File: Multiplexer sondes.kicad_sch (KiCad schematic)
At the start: 4 parts

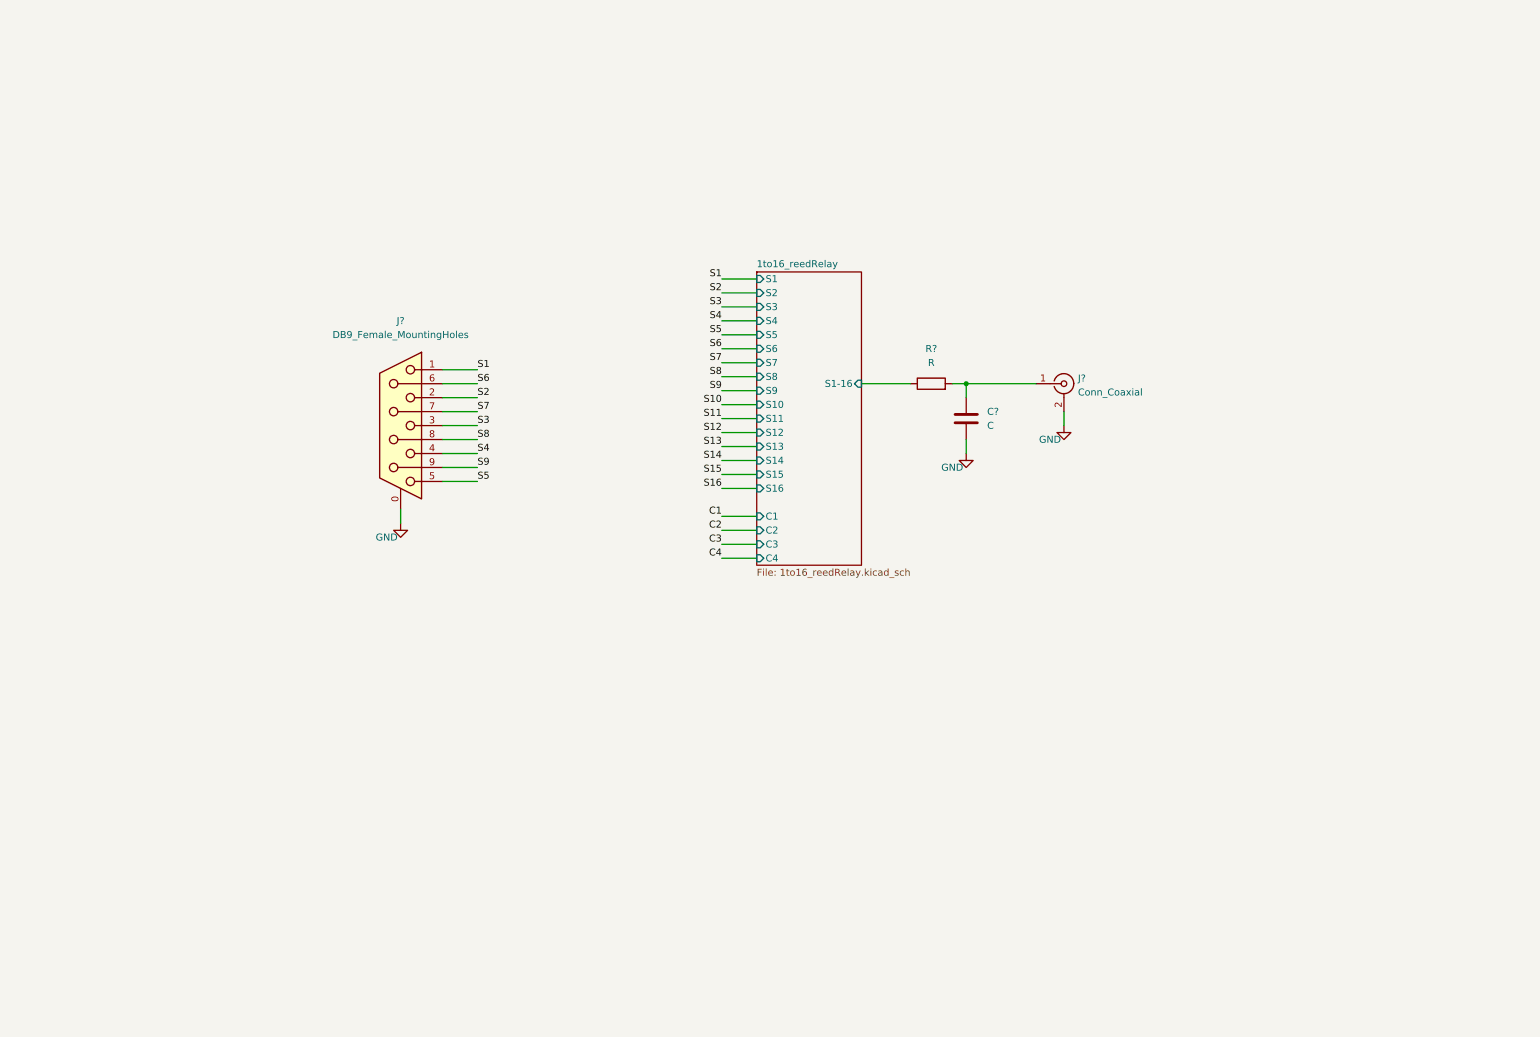
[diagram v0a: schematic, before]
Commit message: Changed to COMUS relay (sch & pcb) 1st placement
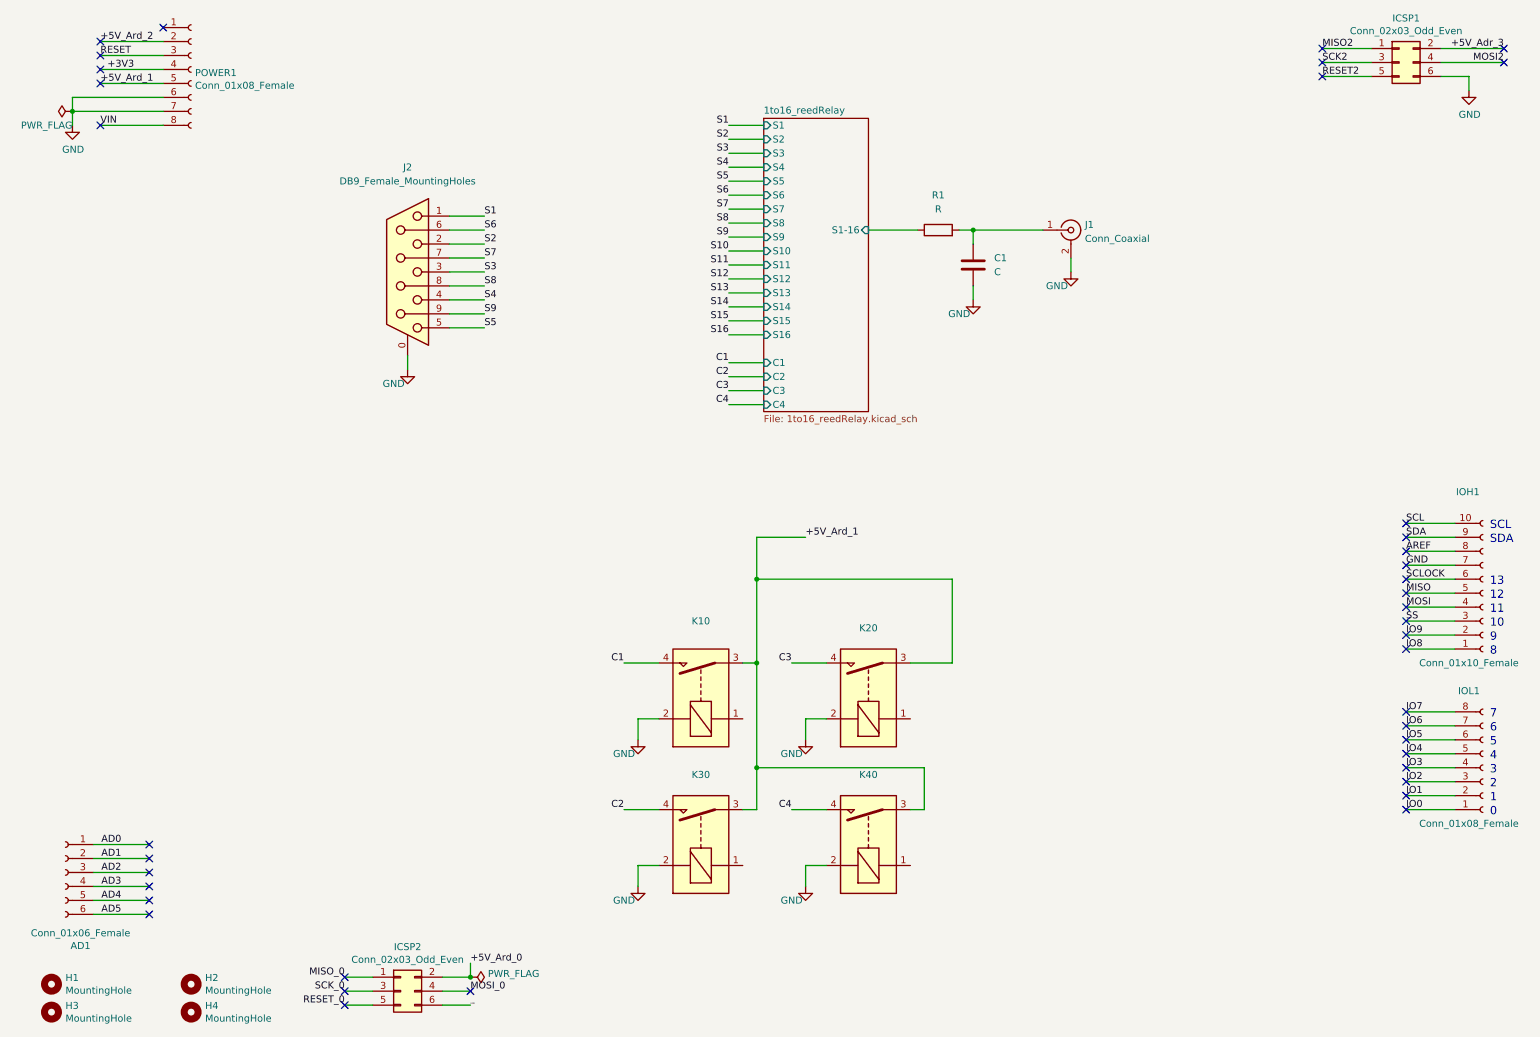
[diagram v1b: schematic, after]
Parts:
- added AD1: Conn_01x06_Female, Connector_PinHeader_2.54mm:PinHeader_1x06_P2.54mm_Vertical, symbol Connector:Conn_01x06_Female
- added H1, H2, H3, H4: MountingHole, MountingHole:MountingHole_3mm, symbol Mechanical:MountingHole
- added ICSP1, ICSP2: Conn_02x03_Odd_Even, Connector_PinSocket_2.54mm:PinSocket_2x03_P2.54mm_Vertical, symbol Connector_Generic:Conn_02x03_Odd_Even
- added IOH1: Conn_01x10_Female, Connector_PinHeader_2.54mm:PinHeader_1x10_P2.54mm_Vertical, symbol Connector:Conn_01x10_Female
- added IOL1, POWER1: Conn_01x08_Female, Connector_PinHeader_2.54mm:PinHeader_1x08_P2.54mm_Vertical, symbol Connector:Conn_01x08_Female
- added K10, K20, K30, K40: (no value), symbol LibPersoNadj:Relay_reed_SPST_1A_small
- C1: renamed from C?; footprint (none) -> Capacitor_SMD:C_0603_1608Metric_Pad1.08x0.95mm_HandSolder
- J1: renamed from J?; footprint (none) -> Connector_Coaxial:SMA_Molex_73251-2120_EdgeMount_Horizontal
- J2: renamed from J?; footprint (none) -> Connector_Dsub:DSUB-9_Female_Horizontal_P2.77x2.84mm_EdgePinOffset4.94mm_Housed_MountingHolesOffset7.48mm
- R1: renamed from R?; footprint (none) -> Resistor_SMD:R_0603_1608Metric_Pad0.98x0.95mm_HandSolder
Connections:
- net C1: now also K10.4
- net C2: now also K30.4
- net C3: now also K20.4
- net C4: now also K40.4
- net GND: now also ICSP1.6 (Pin_6), ICSP2.6 (Pin_6), IOH1.7 (Pin_7), K10.2, K20.2, K30.2, K40.2, POWER1.6 (Pin_6), POWER1.7 (Pin_7)
- new net +3V3: POWER1.4 (Pin_4)
- new net +5V_Adr_3: ICSP1.2 (Pin_2)
- new net +5V_Ard_0: ICSP2.2 (Pin_2)
- new net +5V_Ard_1: K10.3, K20.3, K30.3, K40.3, POWER1.5 (Pin_5)
- new net +5V_Ard_2: POWER1.2 (Pin_2)
- new net AD0: AD1.1 (Pin_1)
- new net AD1: AD1.2 (Pin_2)
- new net AD2: AD1.3 (Pin_3)
- new net AD3: AD1.4 (Pin_4)
- new net AD4: AD1.5 (Pin_5)
- new net AD5: AD1.6 (Pin_6)
- new net AREF: IOH1.8 (Pin_8)
- new net IO0: IOL1.1 (Pin_1)
- new net IO1: IOL1.2 (Pin_2)
- new net IO2: IOL1.3 (Pin_3)
- new net IO3: IOL1.4 (Pin_4)
- new net IO4: IOL1.5 (Pin_5)
- new net IO5: IOL1.6 (Pin_6)
- new net IO6: IOL1.7 (Pin_7)
- new net IO7: IOL1.8 (Pin_8)
- new net IO8: IOH1.1 (Pin_1)
- new net IO9: IOH1.2 (Pin_2)
- new net MISO: IOH1.5 (Pin_5)
- new net MISO2: ICSP1.1 (Pin_1)
- new net MISO_0: ICSP2.1 (Pin_1)
- new net MOSI: IOH1.4 (Pin_4)
- new net MOSI2: ICSP1.4 (Pin_4)
- new net MOSI_0: ICSP2.4 (Pin_4)
- new net RESET: POWER1.3 (Pin_3)
- new net RESET2: ICSP1.5 (Pin_5)
- new net RESET_0: ICSP2.5 (Pin_5)
- new net SCK2: ICSP1.3 (Pin_3)
- new net SCK_0: ICSP2.3 (Pin_3)
- new net SCL: IOH1.10 (Pin_10)
- new net SCLOCK: IOH1.6 (Pin_6)
- new net SDA: IOH1.9 (Pin_9)
- new net SS: IOH1.3 (Pin_3)
- new net VIN: POWER1.8 (Pin_8)
- no-connect marks 0 -> 39
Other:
- note added: "0"
- note added: "1"
- note added: "10"
- note added: "11"
- note added: "12"
- note added: "13"
- note added: "2"
- note added: "3"
- note added: "4"
- note added: "5"
- note added: "6"
- note added: "7"
- note added: "8"
- note added: "9"
- note added: "SCL"
- note added: "SDA"
- moved on the sheet: C1, J1, J2, R1

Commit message: deleted part of the arduino's pins began routing
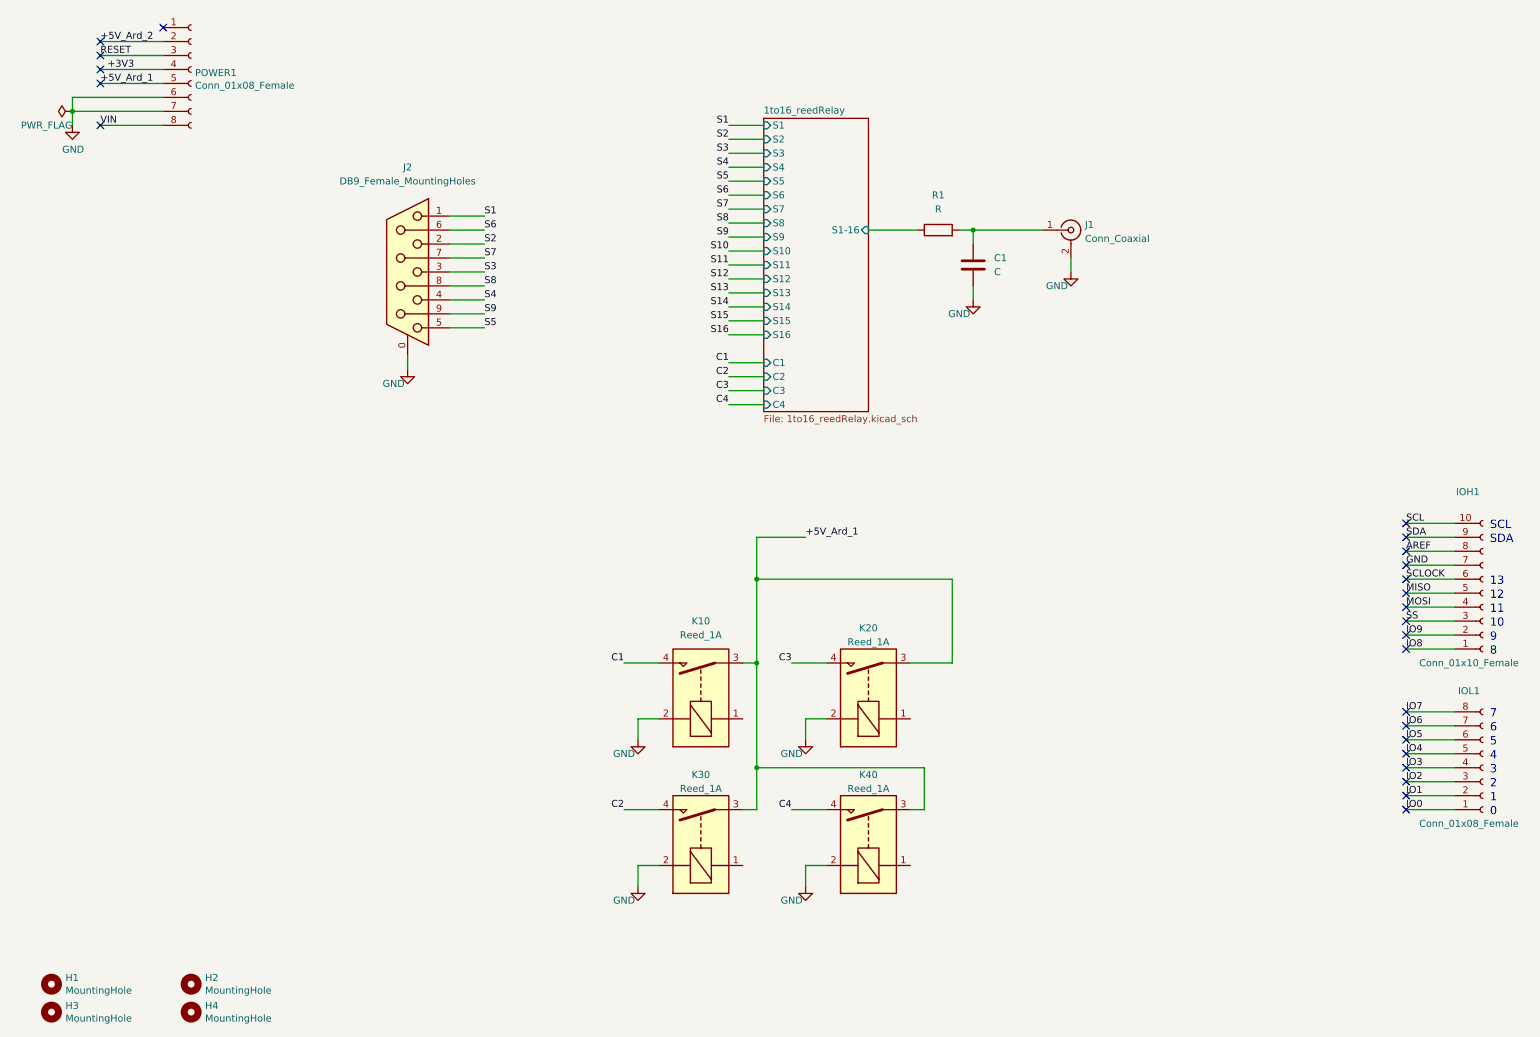
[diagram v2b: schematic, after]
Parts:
- removed AD1: Conn_01x06_Female, Connector_PinHeader_2.54mm:PinHeader_1x06_P2.54mm_Vertical, symbol Connector:Conn_01x06_Female
- removed ICSP1, ICSP2: Conn_02x03_Odd_Even, Connector_PinSocket_2.54mm:PinSocket_2x03_P2.54mm_Vertical, symbol Connector_Generic:Conn_02x03_Odd_Even
- K10, K20, K30, K40: value (none) -> Reed_1A; footprint (none) -> LibPersoNadj:Relay_reed_comus_3570-1517
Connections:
- no-connect marks 39 -> 24

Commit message: Passed to 1 relay per signal with Arduino Mega
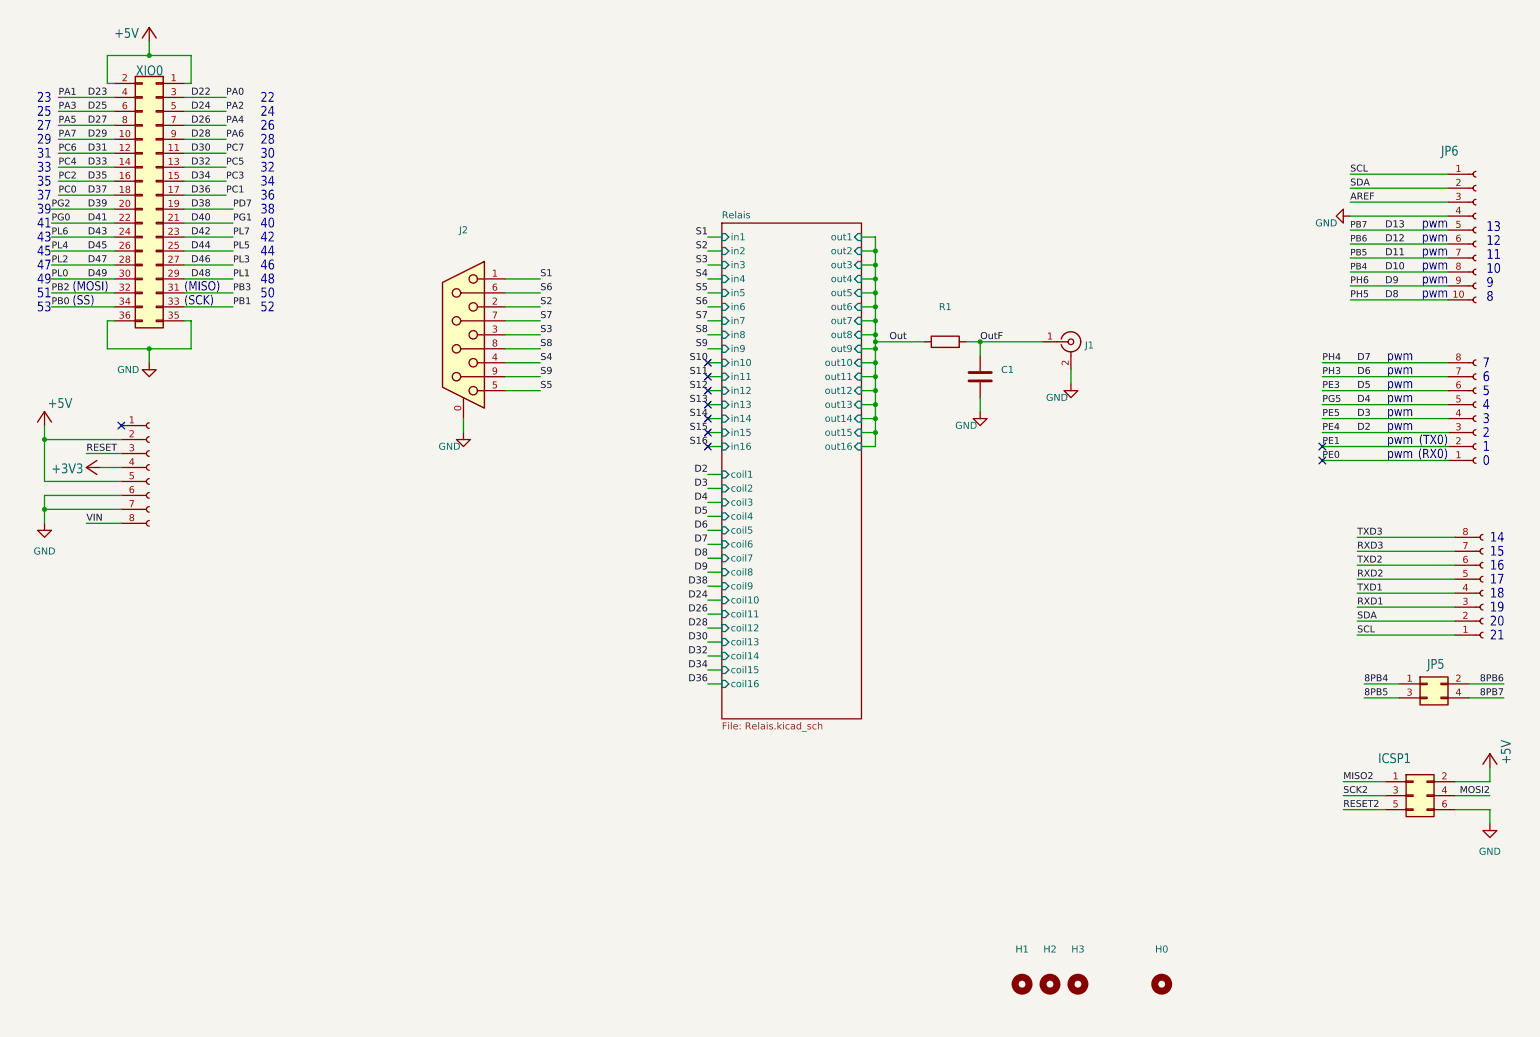
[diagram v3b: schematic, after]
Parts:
- removed H4: MountingHole, MountingHole:MountingHole_3mm, symbol Mechanical:MountingHole
- removed IOH1: Conn_01x10_Female, Connector_PinHeader_2.54mm:PinHeader_1x10_P2.54mm_Vertical, symbol Connector:Conn_01x10_Female
- removed IOL1, POWER1: Conn_01x08_Female, Connector_PinHeader_2.54mm:PinHeader_1x08_P2.54mm_Vertical, symbol Connector:Conn_01x08_Female
- removed K10, K20, K30, K40: Reed_1A, LibPersoNadj:Relay_reed_comus_3570-1517, symbol LibPersoNadj:Relay_reed_SPST_1A_small
- added COMMUNICATION0, POWER0, PWML0: (no value), symbol Connector:Conn_01x08_Female
- added H0: (no value), symbol Mechanical:MountingHole
- added ICSP1: (no value), symbol Connector_Generic:Conn_02x03_Odd_Even
- added JP5: (no value), symbol Connector_Generic:Conn_02x02_Odd_Even
- added JP6: (no value), symbol Connector:Conn_01x10_Female
- added XIO0: (no value), symbol Connector_Generic:Conn_02x18_Odd_Even
- C1: value C -> (none); footprint Capacitor_SMD:C_0603_1608Metric_Pad1.08x0.95mm_HandSolder -> (none)
- H1, H2, H3: value MountingHole -> (none); footprint MountingHole:MountingHole_3mm -> (none)
- J1: value Conn_Coaxial -> (none); footprint Connector_Coaxial:SMA_Molex_73251-2120_EdgeMount_Horizontal -> (none)
- J2: value DB9_Female_MountingHoles -> (none); footprint Connector_Dsub:DSUB-9_Female_Horizontal_P2.77x2.84mm_EdgePinOffset4.94mm_Housed_MountingHolesOffset7.48mm -> (none)
- R1: value R -> (none); footprint Resistor_SMD:R_0603_1608Metric_Pad0.98x0.95mm_HandSolder -> (none)
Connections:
- net +3V3: now also POWER0.4 (Pin_4)
- net AREF: now also JP6.3 (Pin_3)
- net GND: now also ICSP1.6 (Pin_6), JP6.4 (Pin_4), POWER0.6 (Pin_6), POWER0.7 (Pin_7), XIO0.35 (Pin_35), XIO0.36 (Pin_36)
- net RESET: now also POWER0.3 (Pin_3)
- net SCL: now also COMMUNICATION0.1 (Pin_1), JP6.1 (Pin_1)
- net SDA: now also COMMUNICATION0.2 (Pin_2), JP6.2 (Pin_2)
- net VIN: now also POWER0.8 (Pin_8)
- net OutF: now reaches C1.1, J1.1 (In), R1.2
- net 1to16_reedRelay/S1-16 renamed Out
- new net +5V: ICSP1.2 (Pin_2), POWER0.2 (Pin_2), POWER0.5 (Pin_5), XIO0.1 (Pin_1), XIO0.2 (Pin_2)
- new net 8PB4: JP5.1 (Pin_1)
- new net 8PB5: JP5.3 (Pin_3)
- new net 8PB6: JP5.2 (Pin_2)
- new net 8PB7: JP5.4 (Pin_4)
- new net D10: JP6.8 (Pin_8)
- new net D11: JP6.7 (Pin_7)
- new net D12: JP6.6 (Pin_6)
- new net D13: JP6.5 (Pin_5)
- new net D2: PWML0.3 (Pin_3)
- new net D22: XIO0.3 (Pin_3)
- new net D23: XIO0.4 (Pin_4)
- new net D24: XIO0.5 (Pin_5)
- new net D25: XIO0.6 (Pin_6)
- new net D26: XIO0.7 (Pin_7)
- new net D27: XIO0.8 (Pin_8)
- new net D28: XIO0.9 (Pin_9)
- new net D29: XIO0.10 (Pin_10)
- new net D3: PWML0.4 (Pin_4)
- new net D30: XIO0.11 (Pin_11)
- new net D31: XIO0.12 (Pin_12)
- new net D32: XIO0.13 (Pin_13)
- new net D33: XIO0.14 (Pin_14)
- new net D34: XIO0.15 (Pin_15)
- new net D35: XIO0.16 (Pin_16)
- new net D36: XIO0.17 (Pin_17)
- new net D37: XIO0.18 (Pin_18)
- new net D38: XIO0.19 (Pin_19)
- new net D39: XIO0.20 (Pin_20)
- new net D4: PWML0.5 (Pin_5)
- new net D40: XIO0.21 (Pin_21)
- new net D41: XIO0.22 (Pin_22)
- new net D42: XIO0.23 (Pin_23)
- new net D43: XIO0.24 (Pin_24)
- new net D44: XIO0.25 (Pin_25)
- new net D45: XIO0.26 (Pin_26)
- new net D46: XIO0.27 (Pin_27)
- new net D47: XIO0.28 (Pin_28)
- new net D48: XIO0.29 (Pin_29)
- new net D49: XIO0.30 (Pin_30)
- new net D5: PWML0.6 (Pin_6)
- new net D6: PWML0.7 (Pin_7)
- new net D7: PWML0.8 (Pin_8)
- new net D8: JP6.10 (Pin_10)
- new net D9: JP6.9 (Pin_9)
- new net MISO2: ICSP1.1 (Pin_1)
- new net MOSI2: ICSP1.4 (Pin_4)
- new net PB0: XIO0.34 (Pin_34)
- new net PB1: XIO0.33 (Pin_33)
- new net PB2: XIO0.32 (Pin_32)
- new net PB3: XIO0.31 (Pin_31)
- new net PE0: PWML0.1 (Pin_1)
- new net PE1: PWML0.2 (Pin_2)
- new net RESET2: ICSP1.5 (Pin_5)
- new net RXD1: COMMUNICATION0.3 (Pin_3)
- new net RXD2: COMMUNICATION0.5 (Pin_5)
- new net RXD3: COMMUNICATION0.7 (Pin_7)
- new net SCK2: ICSP1.3 (Pin_3)
- new net TXD1: COMMUNICATION0.4 (Pin_4)
- new net TXD2: COMMUNICATION0.6 (Pin_6)
- new net TXD3: COMMUNICATION0.8 (Pin_8)
- no-connect marks 24 -> 10
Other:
- removed sheet 1to16_reedRelay
- added sheet Relais (Relais.kicad_sch)
- note added: "(MISO)"
- note added: "(MOSI)"
- note added: "(RX0)"
- note added: "(SCK)"
- note added: "(SS)"
- note added: "(TX0)"
- note added: "14"
- note added: "15"
- note added: "16"
- note added: "17"
- note added: "18"
- note added: "19"
- note added: "20"
- note added: "21"
- note added: "22"
- note added: "23"
- note added: "24"
- note added: "25"
- note added: "26"
- note added: "27"
- note added: "28"
- note added: "29"
- note added: "30"
- note added: "31"
- note added: "32"
- note added: "33"
- note added: "34"
- note added: "35"
- note added: "36"
- note added: "37"
- note added: "38"
- note added: "39"
- note added: "40"
- note added: "41"
- note added: "42"
- note added: "43"
- note added: "44"
- note added: "45"
- note added: "46"
- note added: "47"
- note added: "48"
- note added: "49"
- note added: "50"
- note added: "51"
- note added: "52"
- note added: "53"
- note added: "pwm"
- note removed: "SCL"
- note removed: "SDA"
- moved on the sheet: J2
